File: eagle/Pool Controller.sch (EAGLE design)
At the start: 25 parts, among them J1 POWER_JACKPTH, J2 Temp_Pool, J4 Solar_Mon, J5 Temp_Solar, J6 Temp_Roof

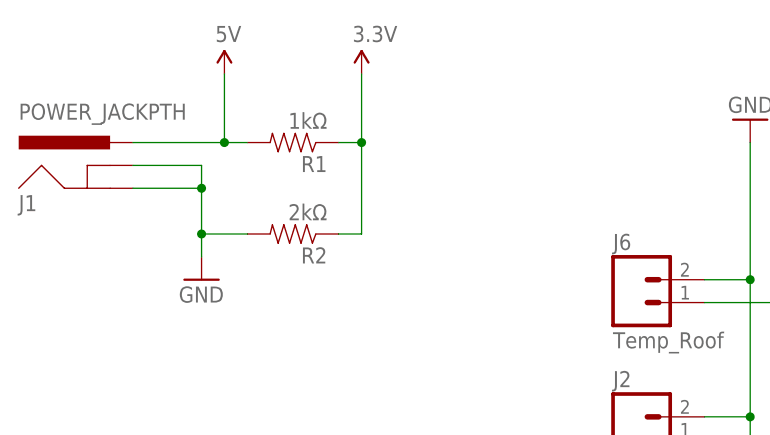
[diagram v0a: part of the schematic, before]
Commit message: Added 3.3v Regulator
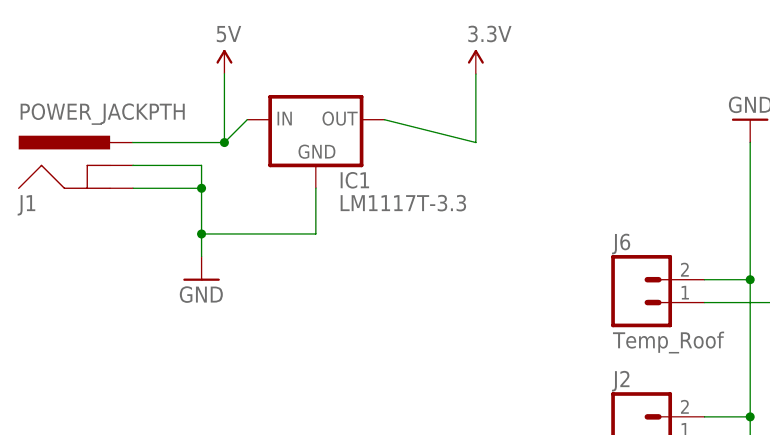
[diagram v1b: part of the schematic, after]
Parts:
- removed R1: 1kΩ, SparkFun-Passives:RESISTORAXIAL-0.3
- removed R2: 2kΩ, SparkFun-Passives:RESISTORAXIAL-0.3
- added IC1: LM1117T-3.3, lm1117:LM1117T-3.3-V
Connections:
- net 3.3V: now also IC1.OUT; no longer R1.1, R2.1
- net 5V: now also IC1.IN; no longer R1.2
- net GND: now also IC1.GND; no longer R2.2
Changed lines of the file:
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@@
 <part name="FRAME1" library="frames" deviceset="LETTER_L" device=""/>
 <part name="J1" library="SparkFun-Connectors" deviceset="POWER_JACK" device="PTH"/>
-<part name="R1" library="SparkFun-Passives" deviceset="RESISTOR" device="AXIAL-0.3" value="1kΩ"/>
-<part name="R2" library="SparkFun-Passives" deviceset="RESISTOR" device="AXIAL-0.3" value="2kΩ"/>
 <part name="R4" library="SparkFun-Sensors" deviceset="PHOTOCELL" device="PTH" value="PHOTOCELL"/>
 <part name="R5" library="SparkFun-Passives" deviceset="RESISTOR" device="AXIAL-0.3" value="10kΩ"/>
@@
 <part name="J6" library="SparkFun-Connectors" deviceset="M02" device="5MM" value="Temp_Roof"/>
 <part name="R11" library="SparkFun-Passives" deviceset="RESISTOR" device="AXIAL-0.3" value="10kΩ"/>
+<part name="IC1" library="lm1117" deviceset="LM1117T-*" device="-V" technology="3.3" value="LM1117T-3.3"/>
 </parts>
 <sheets>
@@
 <instance part="FRAME1" gate="G$2" x="142.24" y="-45.72"/>
 <instance part="J1" gate="G$1" x="15.24" y="111.76"/>
-<instance part="R1" gate="G$1" x="35.56" y="119.38" rot="R180"/>
-<instance part="R2" gate="G$1" x="35.56" y="109.22" rot="R180"/>
 <instance part="R4" gate="G$1" x="55.88" y="71.12"/>
 <instance part="R5" gate="G$1" x="55.88" y="55.88"/>
 <instance part="GND1" gate="1" x="25.4" y="104.14"/>
-<instance part="SUPPLY1" gate="G$1" x="43.18" y="127"/>
+<instance part="SUPPLY1" gate="G$1" x="55.88" y="127"/>
 <instance part="SUPPLY2" gate="G$1" x="175.26" y="116.84"/>
 <instance part="GND2" gate="1" x="121.92" y="106.68" rot="R180"/>
@@
 <instance part="J6" gate="G$1" x="73.66" y="101.6"/>
 <instance part="R11" gate="G$1" x="93.98" y="111.76" rot="R270"/>
+<instance part="IC1" gate="G$1" x="38.1" y="121.92"/>
 </instances>
 <busses>
@@
 <wire x1="17.78" y1="114.3" x2="25.4" y2="114.3" width="0.1524" layer="91"/>
 <junction x="25.4" y="114.3"/>
-<pinref part="R2" gate="G$1" pin="2"/>
-<wire x1="30.48" y1="109.22" x2="25.4" y2="109.22" width="0.1524" layer="91"/>
 <junction x="25.4" y="109.22"/>
+<pinref part="IC1" gate="G$1" pin="GND"/>
+<wire x1="38.1" y1="114.3" x2="38.1" y2="109.22" width="0.1524" layer="91"/>
+<wire x1="38.1" y1="109.22" x2="25.4" y2="109.22" width="0.1524" layer="91"/>
 </segment>
 <segment>
@@
 <segment>
 <pinref part="J1" gate="G$1" pin="PWR"/>
-<pinref part="R1" gate="G$1" pin="2"/>
 <wire x1="17.78" y1="119.38" x2="27.94" y2="119.38" width="0.1524" layer="91"/>
 <pinref part="SUPPLY6" gate="G$1" pin="VCC"/>
-<wire x1="27.94" y1="119.38" x2="30.48" y2="119.38" width="0.1524" layer="91"/>
+<wire x1="27.94" y1="119.38" x2="30.48" y2="121.92" width="0.1524" layer="91"/>
 <wire x1="27.94" y1="127" x2="27.94" y2="119.38" width="0.1524" layer="91"/>
 <junction x="27.94" y="119.38"/>
+<pinref part="IC1" gate="G$1" pin="IN"/>
 </segment>
 <segment>
@@
 </segment>
 <segment>
-<pinref part="R2" gate="G$1" pin="1"/>
-<wire x1="40.64" y1="109.22" x2="43.18" y2="109.22" width="0.1524" layer="91"/>
-<wire x1="43.18" y1="109.22" x2="43.18" y2="119.38" width="0.1524" layer="91"/>
 <pinref part="SUPPLY1" gate="G$1" pin="VCC"/>
-<pinref part="R1" gate="G$1" pin="1"/>
-<wire x1="43.18" y1="119.38" x2="43.18" y2="127" width="0.1524" layer="91"/>
-<wire x1="40.64" y1="119.38" x2="43.18" y2="119.38" width="0.1524" layer="91"/>
-<junction x="43.18" y="119.38"/>
-</segment>
-<segment>
+<wire x1="55.88" y1="119.38" x2="55.88" y2="127" width="0.1524" layer="91"/>
+<pinref part="IC1" gate="G$1" pin="OUT"/>
+<wire x1="55.88" y1="119.38" x2="45.72" y2="121.92" width="0.1524" layer="91"/>
+</segment>
+<segment>

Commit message: Revert "Added 3.3v Regulator"
This reverts commit 23a2b24274d4a83250f4b2e9a9d27c3bcc80a4d5.
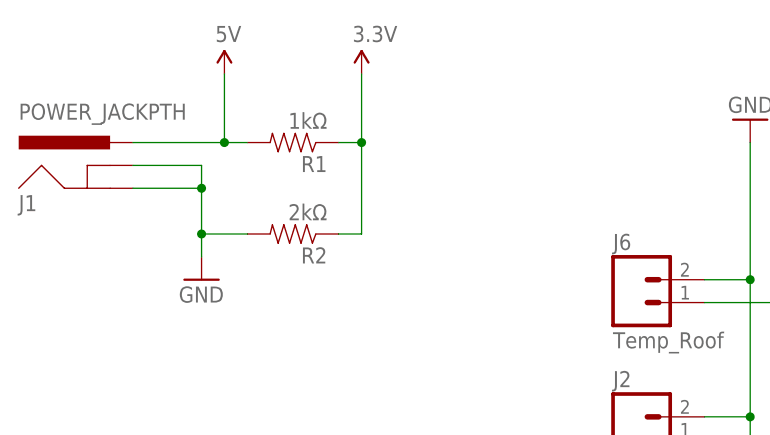
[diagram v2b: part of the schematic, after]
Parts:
- removed IC1: LM1117T-3.3, lm1117:LM1117T-3.3-V
- added R1: 1kΩ, SparkFun-Passives:RESISTORAXIAL-0.3
- added R2: 2kΩ, SparkFun-Passives:RESISTORAXIAL-0.3
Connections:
- net 3.3V: now also R1.1, R2.1; no longer IC1.OUT
- net 5V: now also R1.2; no longer IC1.IN
- net GND: now also R2.2; no longer IC1.GND
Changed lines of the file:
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@@
 <part name="FRAME1" library="frames" deviceset="LETTER_L" device=""/>
 <part name="J1" library="SparkFun-Connectors" deviceset="POWER_JACK" device="PTH"/>
+<part name="R1" library="SparkFun-Passives" deviceset="RESISTOR" device="AXIAL-0.3" value="1kΩ"/>
+<part name="R2" library="SparkFun-Passives" deviceset="RESISTOR" device="AXIAL-0.3" value="2kΩ"/>
 <part name="R4" library="SparkFun-Sensors" deviceset="PHOTOCELL" device="PTH" value="PHOTOCELL"/>
 <part name="R5" library="SparkFun-Passives" deviceset="RESISTOR" device="AXIAL-0.3" value="10kΩ"/>
@@
 <part name="J6" library="SparkFun-Connectors" deviceset="M02" device="5MM" value="Temp_Roof"/>
 <part name="R11" library="SparkFun-Passives" deviceset="RESISTOR" device="AXIAL-0.3" value="10kΩ"/>
-<part name="IC1" library="lm1117" deviceset="LM1117T-*" device="-V" technology="3.3" value="LM1117T-3.3"/>
 </parts>
 <sheets>
@@
 <instance part="FRAME1" gate="G$2" x="142.24" y="-45.72"/>
 <instance part="J1" gate="G$1" x="15.24" y="111.76"/>
+<instance part="R1" gate="G$1" x="35.56" y="119.38" rot="R180"/>
+<instance part="R2" gate="G$1" x="35.56" y="109.22" rot="R180"/>
 <instance part="R4" gate="G$1" x="55.88" y="71.12"/>
 <instance part="R5" gate="G$1" x="55.88" y="55.88"/>
 <instance part="GND1" gate="1" x="25.4" y="104.14"/>
-<instance part="SUPPLY1" gate="G$1" x="55.88" y="127"/>
+<instance part="SUPPLY1" gate="G$1" x="43.18" y="127"/>
 <instance part="SUPPLY2" gate="G$1" x="175.26" y="116.84"/>
 <instance part="GND2" gate="1" x="121.92" y="106.68" rot="R180"/>
@@
 <instance part="J6" gate="G$1" x="73.66" y="101.6"/>
 <instance part="R11" gate="G$1" x="93.98" y="111.76" rot="R270"/>
-<instance part="IC1" gate="G$1" x="38.1" y="121.92"/>
 </instances>
 <busses>
@@
 <wire x1="17.78" y1="114.3" x2="25.4" y2="114.3" width="0.1524" layer="91"/>
 <junction x="25.4" y="114.3"/>
+<pinref part="R2" gate="G$1" pin="2"/>
+<wire x1="30.48" y1="109.22" x2="25.4" y2="109.22" width="0.1524" layer="91"/>
 <junction x="25.4" y="109.22"/>
-<pinref part="IC1" gate="G$1" pin="GND"/>
-<wire x1="38.1" y1="114.3" x2="38.1" y2="109.22" width="0.1524" layer="91"/>
-<wire x1="38.1" y1="109.22" x2="25.4" y2="109.22" width="0.1524" layer="91"/>
 </segment>
 <segment>
@@
 <segment>
 <pinref part="J1" gate="G$1" pin="PWR"/>
+<pinref part="R1" gate="G$1" pin="2"/>
 <wire x1="17.78" y1="119.38" x2="27.94" y2="119.38" width="0.1524" layer="91"/>
 <pinref part="SUPPLY6" gate="G$1" pin="VCC"/>
-<wire x1="27.94" y1="119.38" x2="30.48" y2="121.92" width="0.1524" layer="91"/>
+<wire x1="27.94" y1="119.38" x2="30.48" y2="119.38" width="0.1524" layer="91"/>
 <wire x1="27.94" y1="127" x2="27.94" y2="119.38" width="0.1524" layer="91"/>
 <junction x="27.94" y="119.38"/>
-<pinref part="IC1" gate="G$1" pin="IN"/>
 </segment>
 <segment>
@@
 </segment>
 <segment>
+<pinref part="R2" gate="G$1" pin="1"/>
+<wire x1="40.64" y1="109.22" x2="43.18" y2="109.22" width="0.1524" layer="91"/>
+<wire x1="43.18" y1="109.22" x2="43.18" y2="119.38" width="0.1524" layer="91"/>
 <pinref part="SUPPLY1" gate="G$1" pin="VCC"/>
-<wire x1="55.88" y1="119.38" x2="55.88" y2="127" width="0.1524" layer="91"/>
-<pinref part="IC1" gate="G$1" pin="OUT"/>
-<wire x1="55.88" y1="119.38" x2="45.72" y2="121.92" width="0.1524" layer="91"/>
-</segment>
-<segment>
+<pinref part="R1" gate="G$1" pin="1"/>
+<wire x1="43.18" y1="119.38" x2="43.18" y2="127" width="0.1524" layer="91"/>
+<wire x1="40.64" y1="119.38" x2="43.18" y2="119.38" width="0.1524" layer="91"/>
+<junction x="43.18" y="119.38"/>
+</segment>
+<segment>
